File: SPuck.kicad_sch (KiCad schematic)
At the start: 12 parts, among them IC1 MAX98357AETE+T, J1 12402012E212A, U1 ESP32-S3-WROOM-2, U2 AMS1117-3.3

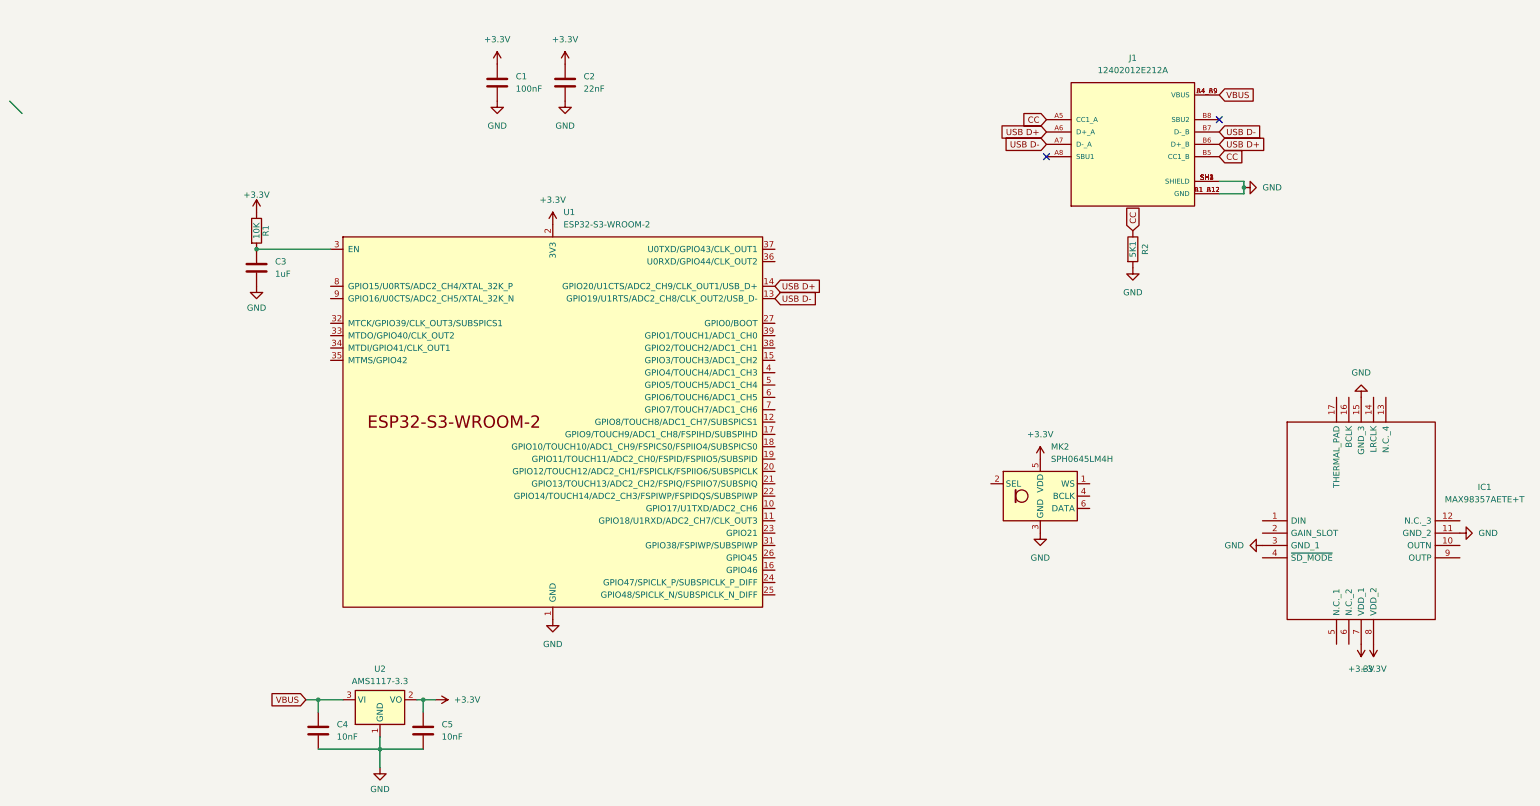
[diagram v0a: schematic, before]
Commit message: Schematic done, PCB WIP
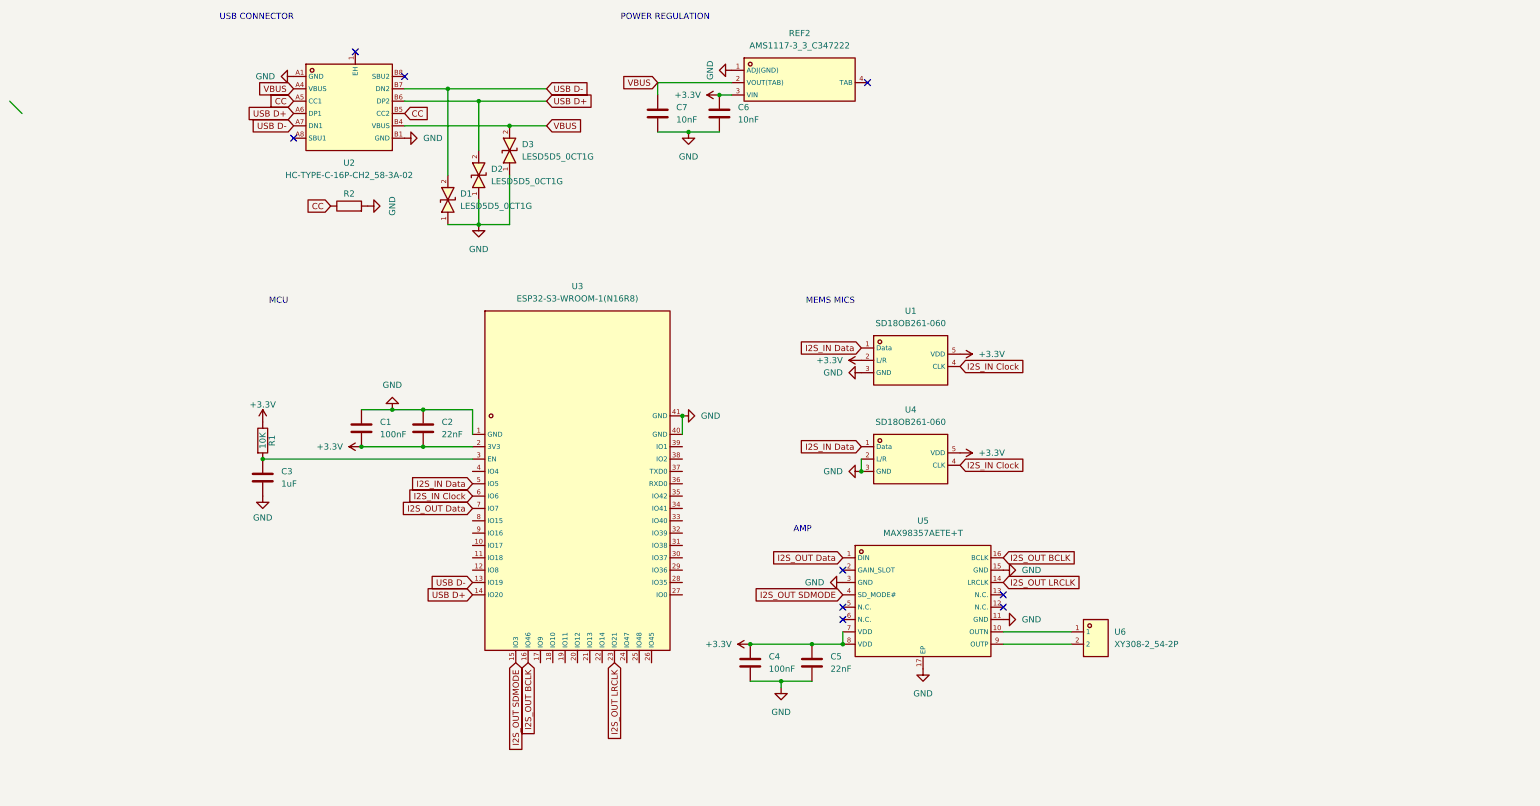
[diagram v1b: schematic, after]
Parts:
- removed IC1: MAX98357AETE+T, QFN50P300X300X80-17N, symbol MAX98357AETE+T:MAX98357AETE+T
- removed J1: 12402012E212A, AMPHENOL_12402012E212A, symbol 12402012E212A:12402012E212A
- removed MK2: SPH0645LM4H, Sensor_Audio:Knowles_SPH0645LM4H-6_3.5x2.65mm, symbol Sensor_Audio:SPH0645LM4H
- removed U1: ESP32-S3-WROOM-2, PCM_Espressif:ESP32-S3-WROOM-2, symbol PCM_Espressif:ESP32-S3-WROOM-2
- removed U2: AMS1117-3.3, Package_TO_SOT_SMD:SOT-223-3_TabPin2, symbol Regulator_Linear:AMS1117-3.3
- added C6, C7: 10nF, Capacitor_SMD:C_0402_1005Metric, symbol Device:C
- added D1, D2, D3: LESD5D5_0CT1G, footprint:SOD-523_L1.2-W0.8-LS1.6-BI, symbol LESD5D5_0CT1G:LESD5D5_0CT1G
- added REF2: AMS1117-3_3_C347222, footprint:SOT-223-4_L6.5-W3.5-P2.30-LS7.0-BR, symbol AMS1117-3_3_C347222:AMS1117-3_3_C347222
- added U1, U4: SD18OB261-060, footprint:MIC-SMD_SD18OB261-060, symbol SD18OB261-060:SD18OB261-060
- added U2: HC-TYPE-C-16P-CH2_58-3A-02, footprint:USB-C-SMD_HC-TYPE-C-16P-CH3.18-3A-02, symbol HC-TYPE-C-16P-CH2_58-3A-02:HC-TYPE-C-16P-CH2_58-3A-02
- added U3: ESP32-S3-WROOM-1(N16R8), footprint:WIRELM-SMD_ESP32-S3-WROOM-1, symbol ESP32-S3-WROOM-1(N16R8):ESP32-S3-WROOM-1(N16R8)
- added U5: MAX98357AETE+T, footprint:TQFN-16_L3.0-W3.0-P0.50-BL-EP1.5, symbol MAX98357AETE+T:MAX98357AETE+T
- added U6: XY308-2_54-2P, footprint:CONN-TH_XY308-2.54-2P, symbol XY308-2_54-2P:XY308-2_54-2P
- C4: value 10nF -> 100nF
- C5: value 10nF -> 22nF
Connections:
- net +3.3V: now also C1.2, C2.2, C4.1, C6.1, REF2.3 (VIN), U1.2 (L/R), U1.5 (VDD), U3.2 (3V3), U4.5 (VDD), U5.7 (VDD), U5.8 (VDD); no longer C1.1, C2.1
- net CC: now also U2.A5 (CC1), U2.B5 (CC2)
- net GND: now also C1.1, C2.1, C6.2, C7.2, D1.1, D2.1, D3.1, REF2.1 (ADJ(GND)), U1.3 (GND), U2.A1 (GND), U2.B1 (GND), U3.1 (GND), U3.40 (GND), U3.41 (GND), U4.2 (L/R), U4.3 (GND), U5.11 (GND), U5.15 (GND), U5.17 (EP), U5.3 (GND); no longer C1.2, C2.2
- net USB D+: now also D2.2, U2.A6 (DP1), U2.B6 (DP2), U3.14 (IO20)
- net USB D-: now also D1.2, U2.A7 (DN1), U2.B7 (DN2), U3.13 (IO19)
- net VBUS: now also C7.1, D3.2, REF2.2 (VOUT(TAB)), U2.A4 (VBUS), U2.B4 (VBUS); no longer C4.1
- net at C3.1, R1.2: now also U3.3 (EN)
- new net: U5.10 (OUTN), U6.1
- new net: U5.9 (OUTP), U6.2
- new net I2S_IN Clock: U1.4 (CLK), U3.6 (IO6), U4.4 (CLK)
- new net I2S_IN Data: U1.1 (Data), U3.5 (IO5), U4.1 (Data)
- new net I2S_OUT BCLK: U3.16 (IO46), U5.16 (BCLK)
- new net I2S_OUT Data: U3.7 (IO7), U5.1 (DIN)
- new net I2S_OUT LRCLK: U3.23 (IO21), U5.14 (LRCLK)
- new net I2S_OUT SDMODE: U3.15 (IO3), U5.4 (SD_MODE#)
- no-connect marks 2 -> 9
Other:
- note added: "AMP"
- note added: "MCU"
- note added: "MEMS MICS"
- note added: "POWER REGULATION"
- note added: "USB CONNECTOR"
- moved on the sheet: C1, C2, C3, R1, R2
